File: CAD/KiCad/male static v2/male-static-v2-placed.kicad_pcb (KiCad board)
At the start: 2 copper layers, 50 x 90 mm, 19 parts, among them J1 photosensor, J10 State LED, J11 bar neopixel, J2 dxl male, J3 microphone, J4 photosensor, J5 body neopixel, J6 Speaker, J7 DA15_Plug_MountingHoles, J8 photosensor, J9 photosensor, M1 GF1002 direct module

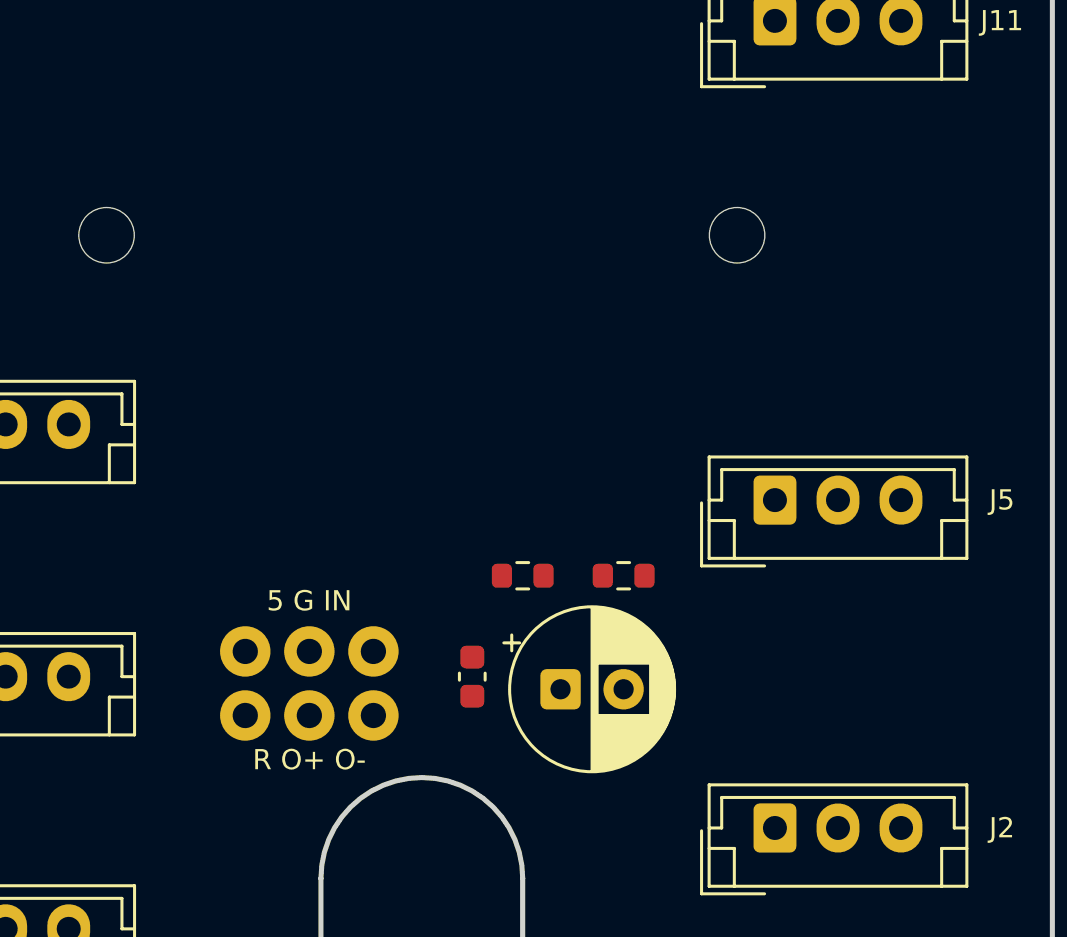
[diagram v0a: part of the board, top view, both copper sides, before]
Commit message: Keep the GF1002 contact row clear on both body boards
Correct the reference to nine contacts on the long edge. Move H2 to the short end, move hookup pads alongside the row, clear nearby components and require flush-cut pin tails. Preserve artwork outlines, DSUB geometry and harness pin order.

Refresh routed PCBs, STEP/VRML models, body scenes, production Gerbers and actual-size templates. User approved the documented dimensional estimates; physical fit and ROUT polarity remain checks before ordering. Native ERC/DRC/parity and clearance checks pass; all 1796 pytest tests pass.
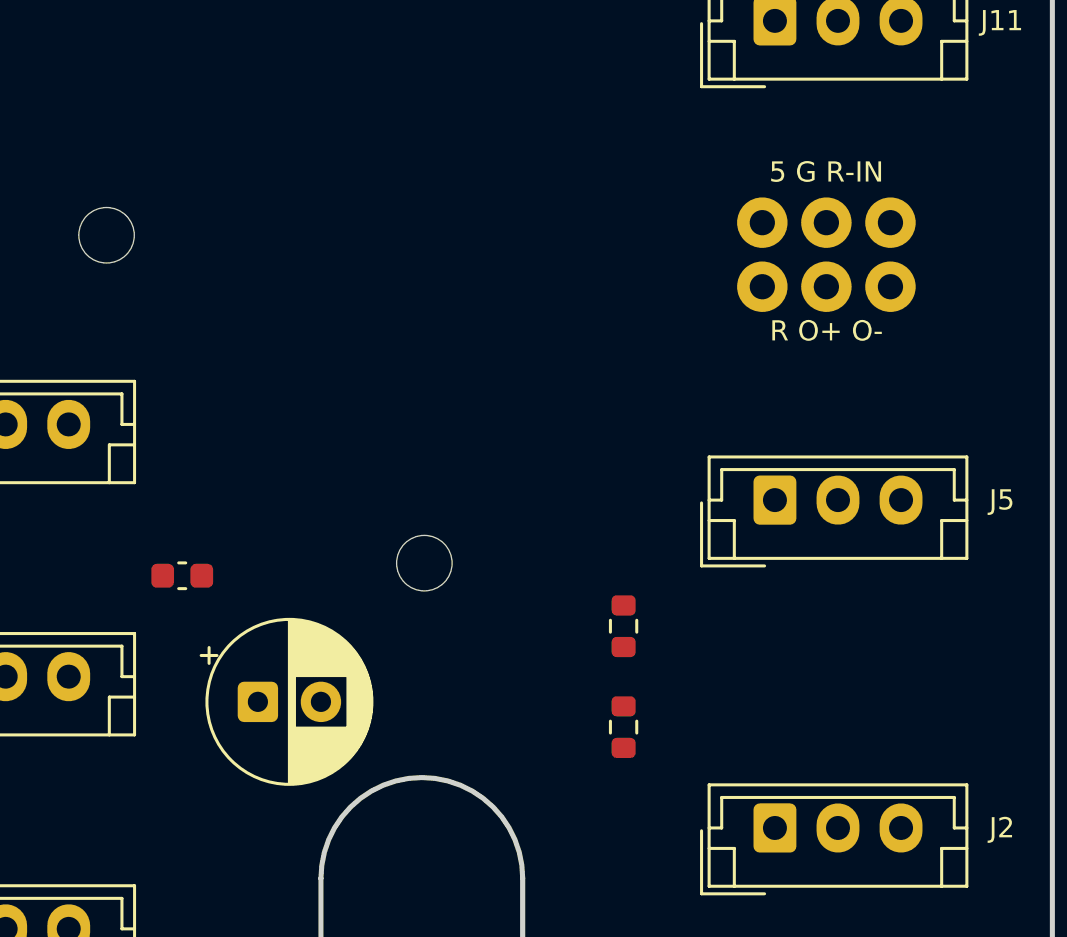
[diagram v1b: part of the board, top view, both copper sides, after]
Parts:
- H2: footprint Body:GF1002_Clamp_Right -> Body:GF1002_Clamp_End
- moved JA1 26.6 mm to (63.5, 74.0)
- moved H2 18.0 mm to (50.1, 87.5), turned to 90 degrees
- moved C2 12.2 mm to (40.5, 88.0), turned to 0 degrees
- moved C1 12.0 mm to (43.5, 93.0)
- moved R2 6.00 mm to (58.0, 94.0), turned to 90 degrees
- moved R1 4.47 mm to (58.0, 90.0), turned to 90 degrees
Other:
- board text added: "5 G R-IN"
- board text added: "TRIM MODULE PINS FLUSH / VERIFY FIT"
- board text removed: "5 G IN"

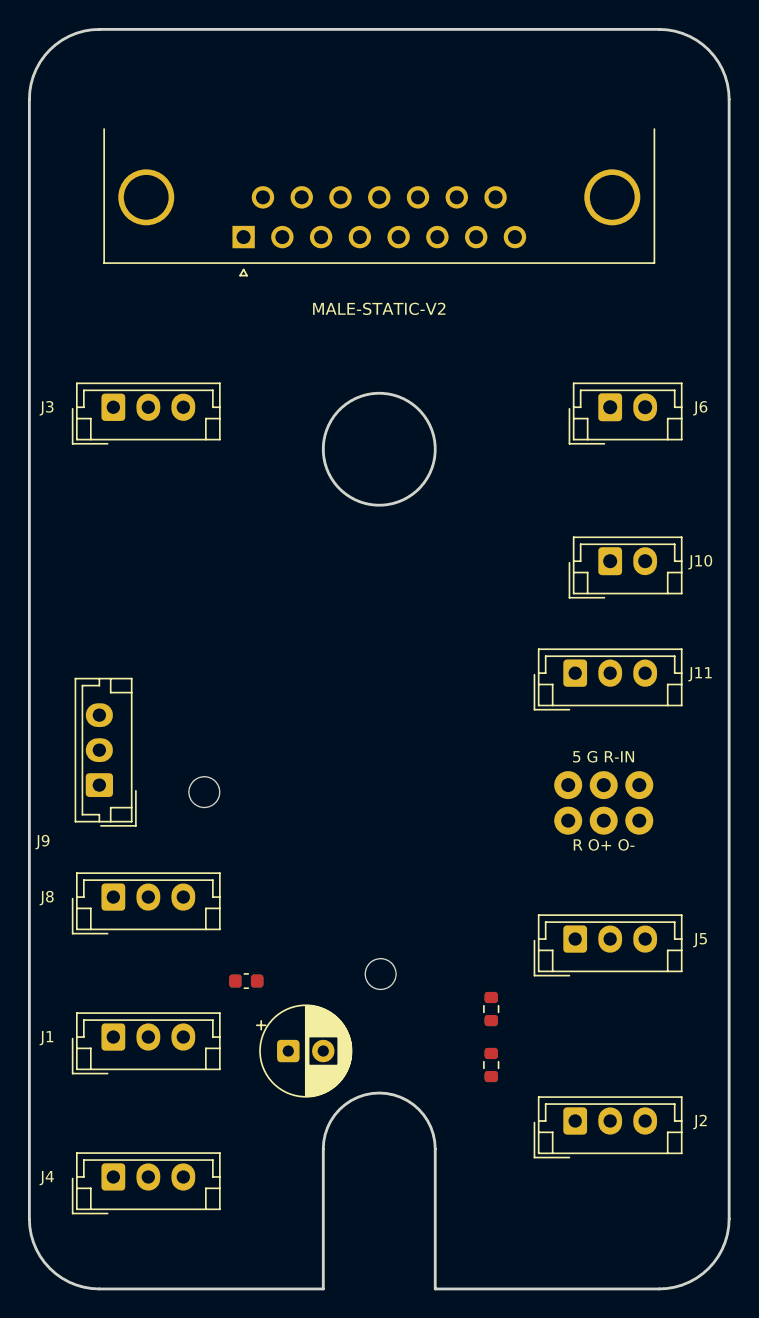
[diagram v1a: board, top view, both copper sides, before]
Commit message: Socket and reroute the body amplifiers to revision D
Replace JA1 wires with eleven-pin GF1002 sockets, explicit unused contacts and an 11 mm header stack. Move the divider and bypass beside their socket pins, shorten and pair the speaker routes, and separate them from audio and sensor inputs with a grounded guard. Add adjustable support models and preserve the artwork outline, DSUB geometry and harness pin order.

Regenerate schematics, routing, models, current body scenes, Gerbers and actual-size templates. Native ERC/DRC/unconnected/parity are zero on both boards; independent socket, support, decoupling and routing checks pass; all 1796 pytest tests pass. Module fit, purchased stack height, module ground bond and ROUT polarity remain physical checks before ordering.
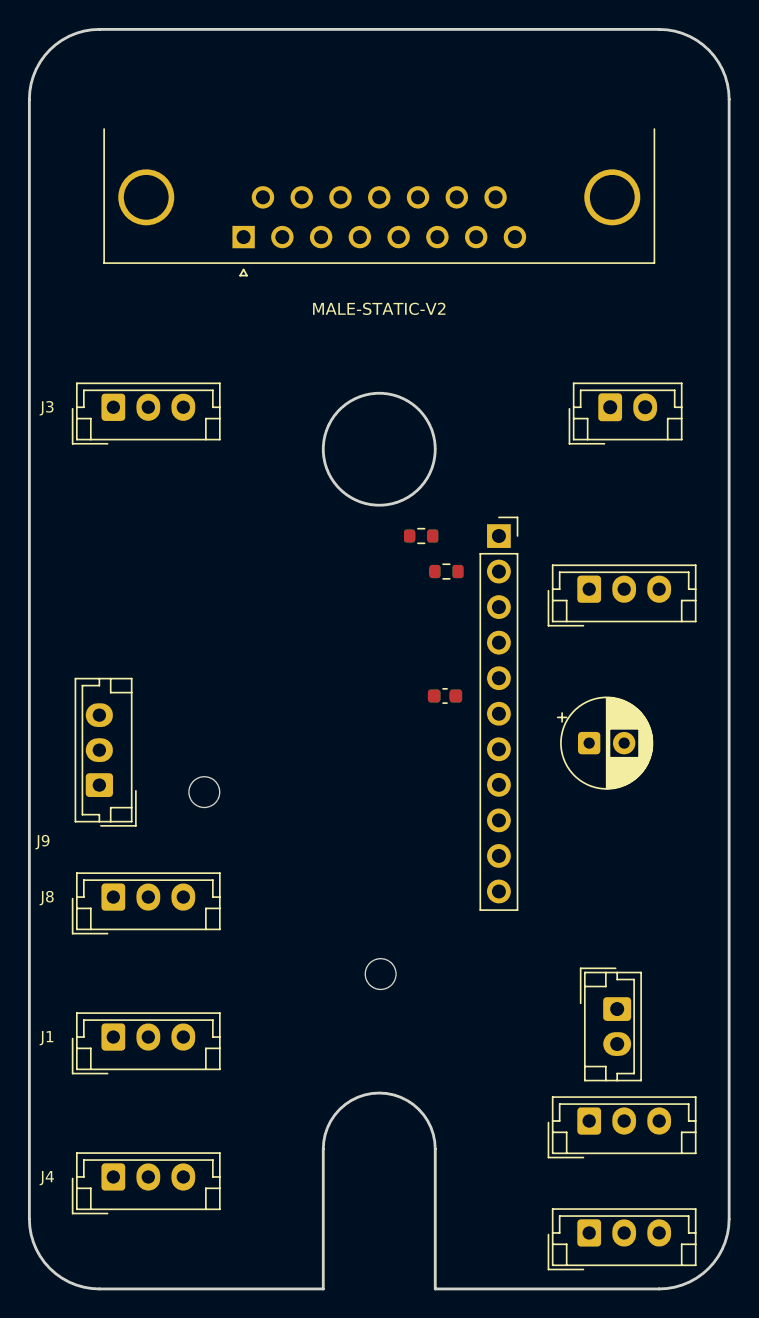
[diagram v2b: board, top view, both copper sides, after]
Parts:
- removed JA1: GF1002 wire connections, Body:GF1002_WirePads_2x03
- H1: value M2 insulating clamp -> M2 insulating support / 11mm; footprint Body:GF1002_Clamp_Left -> Body:GF1002_Support_Left
- H2: value M2 insulating clamp -> M2 insulating support / 11mm; footprint Body:GF1002_Clamp_End -> Body:GF1002_Support_End
- M1: value GF1002 direct module -> GF1002 / 1x11 female socket; footprint Body:GF1002_Module_Direct -> Body:GF1002_PlugIn_1x11
- moved J6 43.0 mm to (67.0, 90.0), turned to -90 degrees
- moved R2 35.4 mm to (54.8, 58.7), turned to 0 degrees
- moved R1 34.2 mm to (53.0, 56.2), turned to 0 degrees
- moved C1 30.8 mm to (65.0, 71.0)
- moved C2 24.8 mm to (54.7, 67.6)
- moved M1 18.6 mm to (58.5, 56.2)
- moved J5 13.0 mm to (65.0, 98.0)
- moved J10 11.0 mm to (66.5, 47.0)
- moved J2 8.06 mm to (65.0, 106.0)
- moved J11 6.08 mm to (65.0, 60.0)
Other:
- board text added: "FIT HEADERS / VERIFY STACK AND POLARITY"
- board text added: "GF1002 / PLUG-IN / 11mm STACK"
- board text added: "R IN"
- board text added: "ROUT +/- VERIFY"
- board text removed: "5 G R-IN"
- board text removed: "GF1002 / DIRECT / NO PERFBOARD"
- board text removed: "R O+ O-"
- board text removed: "TRIM MODULE PINS FLUSH / VERIFY FIT"

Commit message: Use SMD reservoir capacitors on both v2 body boards
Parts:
- C1: footprint Capacitor_THT:CP_Radial_D6.3mm_P2.50mm -> Capacitor_SMD:CP_Elec_6.3x5.8
- moved C1 3.20 mm to (68.2, 71.0)

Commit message: Name every body-board connector on the front silkscreen
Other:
- board text added: "J1 PHOTOSENSOR C"
- board text added: "J10 STATE LED"
- board text added: "J11 BAR NEOPIXEL"
- board text added: "J2 DXL BODY"
- board text added: "J3 MICROPHONE"
- board text added: "J4 PHOTOSENSOR D"
- board text added: "J5 BODY NEOPIXEL"
- board text added: "J6 SPEAKER"
- board text added: "J7 HARNESS"
- board text added: "J8 PHOTOSENSOR B"
- board text added: "J9 PHOTOSENSOR A"
- board text removed: "J1"
- board text removed: "J10"
- board text removed: "J11"
- board text removed: "J2"
- board text removed: "J3"
- board text removed: "J4"
- board text removed: "J5"
- board text removed: "J6"
- board text removed: "J8"
- board text removed: "J9"
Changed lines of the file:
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@@
 		(layer "Edge.Cuts")
 	)
-	(gr_text "J1"
-		(at 26.3 92 0)
+	(gr_text "J6 SPEAKER"
+		(at 62.2 90.5 90)
+		(layer "F.SilkS")
+		(effects
+			(font
+				(size 0.9 0.9)
+				(thickness 0.15)
+			)
+		)
+	)
+	(gr_text "J7 HARNESS"
+		(at 50 38.8 0)
+		(layer "F.SilkS")
+		(effects
+			(font
+				(size 0.9 0.9)
+				(thickness 0.15)
+			)
+		)
+	)
+	(gr_text "J1 PHOTOSENSOR C"
+		(at 33.5 96.3 0)
+		(layer "F.SilkS")
+		(effects
+			(font
+				(size 0.85 0.85)
+				(thickness 0.15)
+			)
+		)
+	)
+	(gr_text "J10 STATE LED"
+		(at 67.5 51.3 0)
+		(layer "F.SilkS")
+		(effects
+			(font
+				(size 0.9 0.9)
+				(thickness 0.15)
+			)
+		)
+	)
+	(gr_text "J8 PHOTOSENSOR B"
+		(at 33.5 86.3 0)
+		(layer "F.SilkS")
+		(effects
+			(font
+				(size 0.85 0.85)
+				(thickness 0.15)
+			)
+		)
+	)
+	(gr_text "J4 PHOTOSENSOR D"
+		(at 33.5 106.3 0)
+		(layer "F.SilkS")
+		(effects
+			(font
+				(size 0.85 0.85)
+				(thickness 0.15)
+			)
+		)
+	)
+	(gr_text "J3 MICROPHONE"
+		(at 33.5 51.3 0)
+		(layer "F.SilkS")
+		(effects
+			(font
+				(size 0.95 0.95)
+				(thickness 0.15)
+			)
+		)
+	)
+	(gr_text "J9 PHOTOSENSOR A"
+		(at 33.5 78.4 0)
+		(layer "F.SilkS")
+		(effects
+			(font
+				(size 0.85 0.85)
+				(thickness 0.15)
+			)
+		)
+	)
+	(gr_text "J2 DXL BODY"
+		(at 67.5 102.3 0)
+		(layer "F.SilkS")
+		(effects
+			(font
+				(size 0.9 0.9)
+				(thickness 0.15)
+			)
+		)
+	)
+	(gr_text "J11 BAR NEOPIXEL"
+		(at 67.5 64.3 0)
+		(layer "F.SilkS")
+		(effects
+			(font
+				(size 0.85 0.85)
+				(thickness 0.15)
+			)
+		)
+	)
+	(gr_text "J5 BODY NEOPIXEL"
+		(at 74.05 98 90)
 		(layer "F.SilkS")
 		(effects
 			(font
 				(size 0.8 0.8)
-				(thickness 0.12)
-			)
-		)
-	)
-	(gr_text "J8"
-		(at 26.3 82 0)
-		(layer "F.SilkS")
-		(effects
-			(font
-				(size 0.8 0.8)
-				(thickness 0.12)
-			)
-		)
-	)
-	(gr_text "J9"
-		(at 26 78 0)
-		(layer "F.SilkS")
-		(effects
-			(font
-				(size 0.8 0.8)
-				(thickness 0.12)
-			)
-		)
-	)
-	(gr_text "J4"
-		(at 26.3 102 0)
-		(layer "F.SilkS")
-		(effects
-			(font
-				(size 0.8 0.8)
-				(thickness 0.12)
-			)
-		)
-	)
-	(gr_text "J3"
-		(at 26.3 47 0)
-		(layer "F.SilkS")
-		(effects
-			(font
-				(size 0.8 0.8)
-				(thickness 0.12)
+				(thickness 0.15)
 			)
 		)
 	)
 	(gr_text "MALE-STATIC-V2"
-		(at 50 40 0)
+		(at 50 41.2 0)
 		(layer "F.SilkS")
 		(effects
@@
 				(thickness 0.12)
 			)
-		)
-	)
-	(gr_text "J11"
-		(at 73 60 0)
-		(layer "F.Fab")
-		(effects
-			(font
-				(size 0.8 0.8)
-				(thickness 0.12)
-			)
-		)
-	)
-	(gr_text "J2"
-		(at 73 106 0)
-		(layer "F.Fab")
-		(effects
-			(font
-				(size 0.8 0.8)
-				(thickness 0.12)
-			)
-		)
-	)
-	(gr_text "J6"
-		(at 73 90 0)
-		(layer "F.Fab")
-		(effects
-			(font
-				(size 0.8 0.8)
-				(thickness 0.12)
-			)
-		)
-	)
-	(gr_text "J10"
-		(at 73 47 0)
-		(layer "F.Fab")
-		(effects
-			(font
-				(size 0.8 0.8)
-				(thickness 0.12)
-			)
-		)
-	)
-	(gr_text "J5"
-		(at 73 98 0)
-		(layer "F.Fab")
-		(effects
-			(font
-				(size 0.8 0.8)
-				(thickness 0.12)
-			)

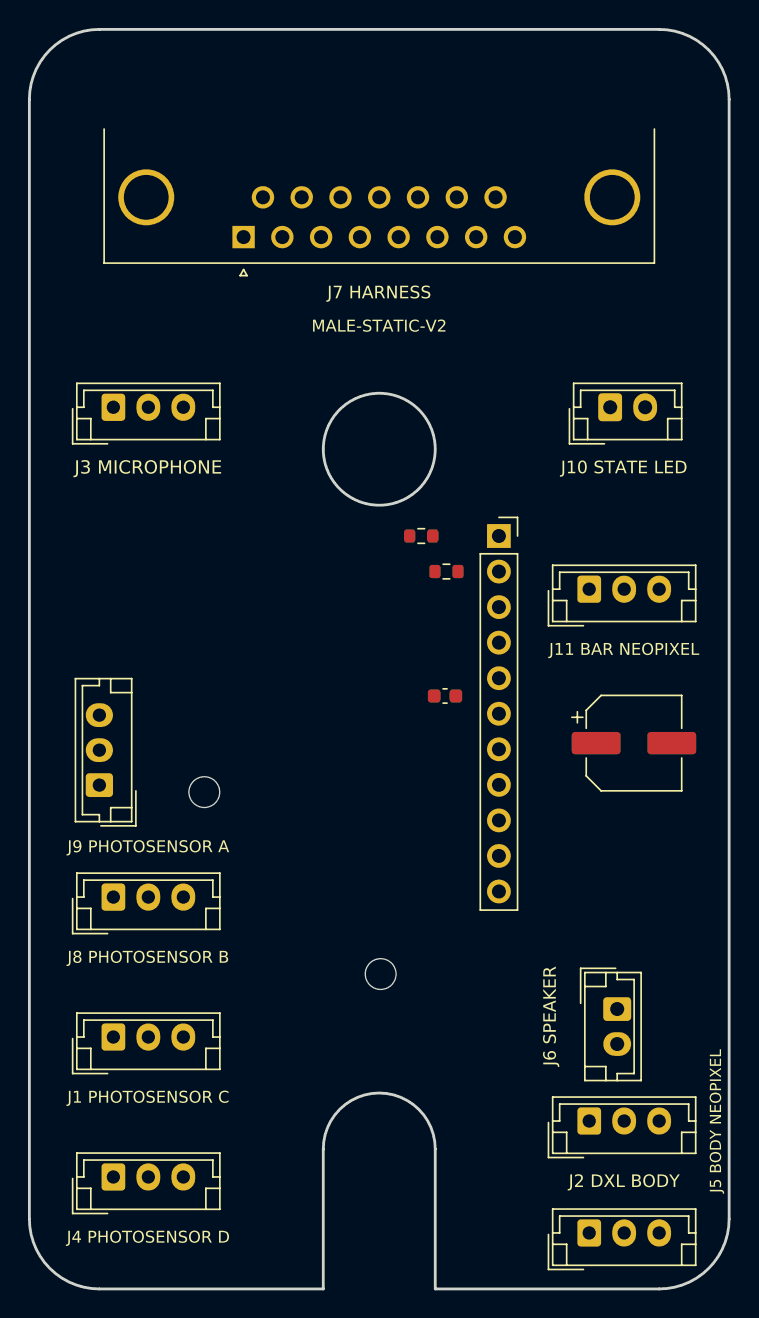
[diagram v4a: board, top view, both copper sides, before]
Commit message: Route male static v2 around the edited component placement
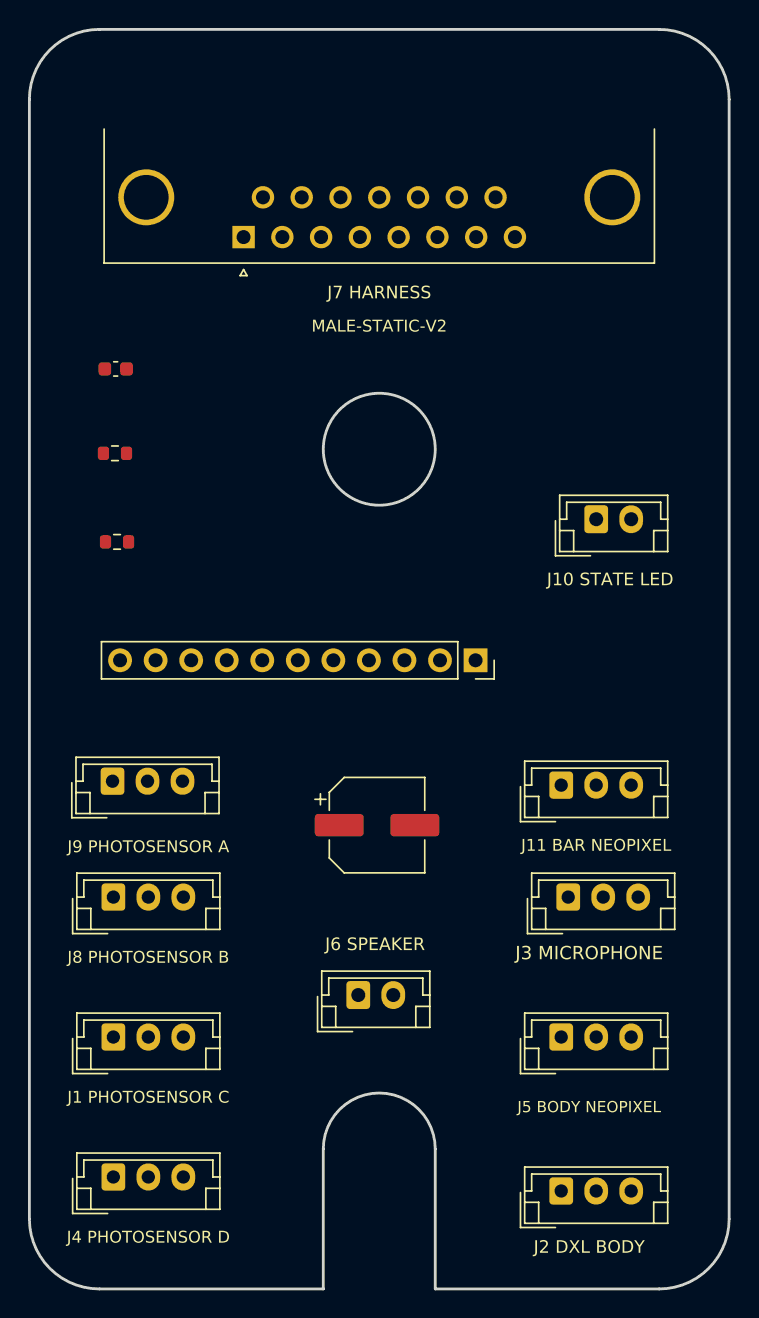
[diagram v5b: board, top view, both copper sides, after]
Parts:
- removed H1: M2 insulating support / 11mm, Body:GF1002_Support_Left
- removed H2: M2 insulating support / 11mm, Body:GF1002_Support_End
- moved J3 47.8 mm to (63.5, 82.0)
- moved C2 33.2 mm to (31.2, 44.3)
- moved R2 23.6 mm to (31.3, 56.6)
- moved R1 22.7 mm to (31.1, 50.3)
- moved C1 19.3 mm to (49.8, 76.9)
- moved J6 18.5 mm to (48.5, 89.0), turned to 0 degrees
- moved J11 14.1 mm to (63.0, 74.0)
- moved M1 9.04 mm to (56.9, 65.1), turned to -90 degrees
- moved J10 8.06 mm to (65.5, 55.0)
- moved J5 6.32 mm to (63.0, 92.0)
- moved J2 3.61 mm to (63.0, 103.0)
- moved J9 0.98 mm to (30.9, 73.7), turned to 0 degrees
